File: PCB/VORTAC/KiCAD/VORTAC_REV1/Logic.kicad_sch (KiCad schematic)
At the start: 36 parts, among them Q3 WSD4066DN, U1 TLV73333PDBV, U4 TPS54335ADRCR

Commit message: hallo
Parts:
- removed C? (x3): 0.1uF 16V, Capacitor_SMD:C_0402_1005Metric, symbol Device:C_Small
- removed Q3: WSD4066DN, ToolChanger:WSD4066DN_ThermalPad, symbol ToolChanger:WSD4066DN
- removed R12, R13, R41, R42, R43, R44, R47, R48, R49, R50: 10K, Resistor_SMD:R_0402_1005Metric, symbol Device:R_Small
- removed R7, R8: 100R, Resistor_SMD:R_0402_1005Metric, symbol Device:R_Small
- added R1, R7: 1K, Resistor_SMD:R_0603_1608Metric, symbol Device:R
- added R2, R8: 2K, Resistor_SMD:R_0603_1608Metric, symbol Device:R
- added R5, R6: 180, Resistor_SMD:R_0603_1608Metric, symbol Device:R
- added S1, S2: ~, ToolChanger:OPB666N, symbol VORTAC_REV1-rescue:OPB666N
- R51: value 10K -> 1K
- gave numbers to parts that had none: 11
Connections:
- net +3V3: now also R5.1, R6.1
- net +5V: now also S1.3 (Vc), S2.3 (Vc)
- net GND: now also R2.2, R8.2, S1.1 (AN), S1.5 (GND), S2.1 (AN), S2.5 (GND)
- net TOOL_ID: now also R51.1; no longer C49.2, R51.2
- net TOOL_ID_PIN: now also C49.2, R51.2; no longer R51.1
- new net: R5.2, S2.2 (CA)
- new net: R7.1, S2.4 (Out)
- new net: R1.1, S1.4 (Out)
- new net: R6.2, S1.2 (CA)
- new net ENDSTOP_X: R7.2, R8.1
- new net ENDSTOP_Z: R1.2, R2.1
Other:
- note removed: "LED/USB MOSFET - WSD4066DN"
- moved on the sheet: C49, R51, R52

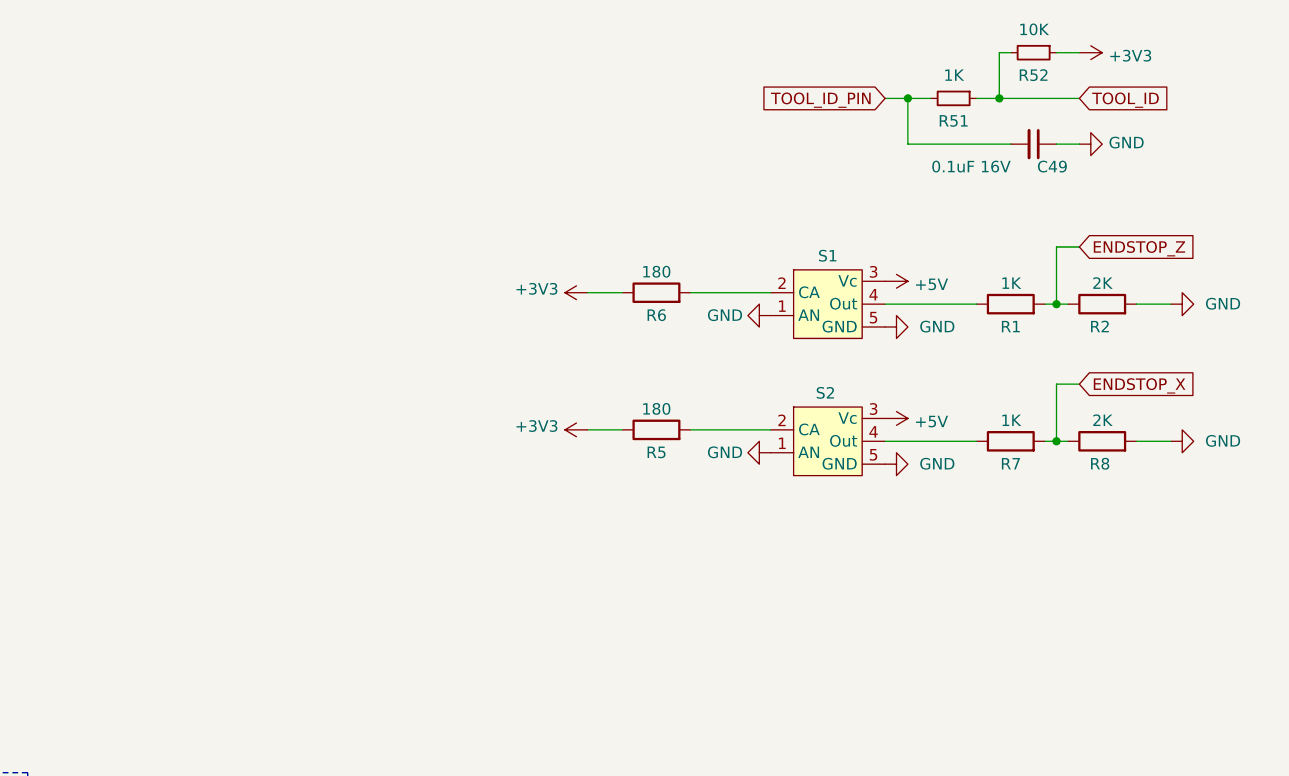
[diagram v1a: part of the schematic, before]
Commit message: Added New EE_SX3350
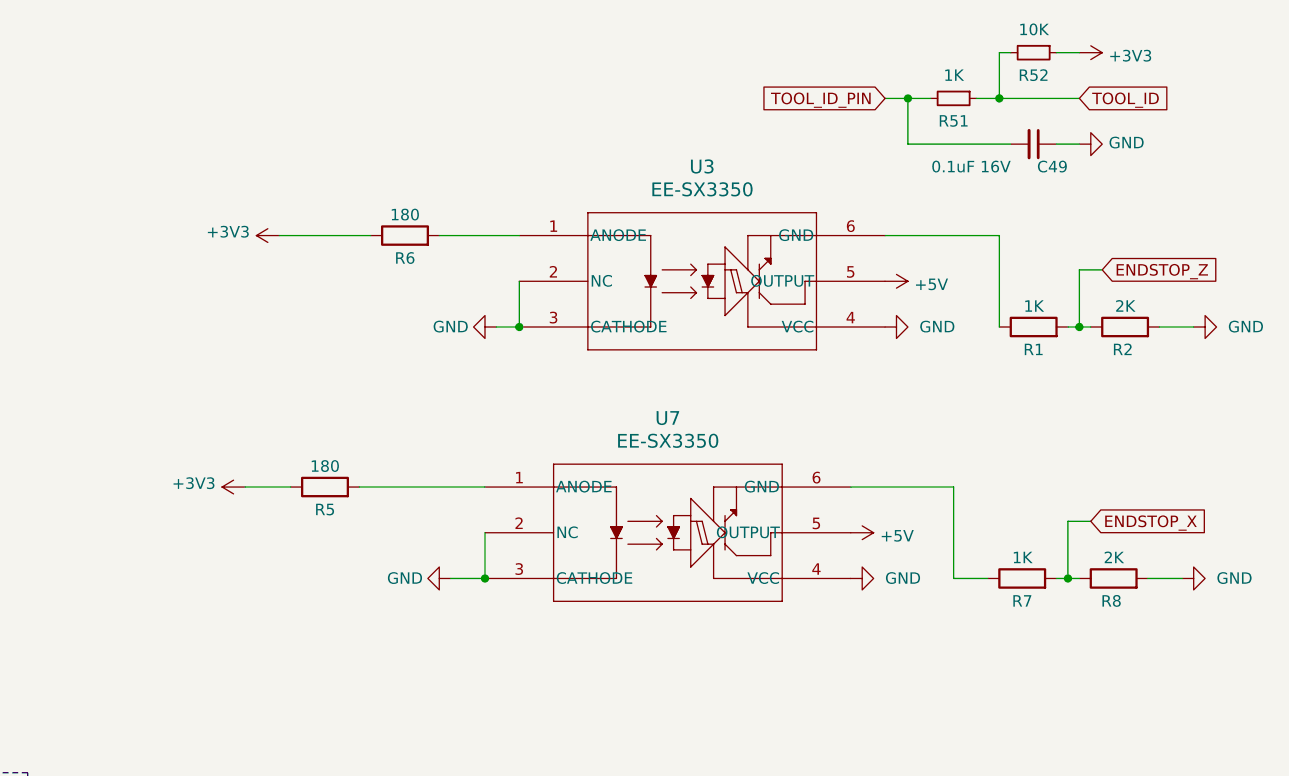
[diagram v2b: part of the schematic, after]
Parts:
- removed S1, S2: ~, ToolChanger:OPB666N, symbol VORTAC_REV1-rescue:OPB666N
- added U3, U7: EE-SX3350, ToolChanger:SENSOR_EE-SX3350_OMR, symbol VORTAC_REV1-rescue:EE-SX3350
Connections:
- net +5V: now also U3.5 (OUTPUT), U7.5 (OUTPUT)
- net GND: now also U3.2 (NC), U3.3 (CATHODE), U3.4 (VCC), U7.2 (NC), U7.3 (CATHODE), U7.4 (VCC)
- net at R5.2: now also U7.1 (ANODE)
- net at R7.1: now also U7.6 (GND)
- net at R1.1: now also U3.6 (GND)
- net at R6.2: now also U3.1 (ANODE)
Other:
- moved on the sheet: R1, R2, R5, R6, R7, R8

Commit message: yipppieee
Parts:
- U3, U7: LCSC (none) -> C7470740
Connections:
- net +5V: now also U3.4 (VCC), U7.4 (VCC); no longer U3.5 (OUTPUT), U7.5 (OUTPUT)
- net GND: now also U3.6 (GND), U7.6 (GND); no longer U3.4 (VCC), U7.4 (VCC)
- net at R7.1: now also U7.5 (OUTPUT); no longer U7.6 (GND)
- net at R1.1: now also U3.5 (OUTPUT); no longer U3.6 (GND)
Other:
- moved on the sheet: C49, R1, R2, R5, R51, R52, R6, R7, R8, U3, U7

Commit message: Fixed Library stuff
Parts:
- L2: footprint ToolChanger:L_Sunlord_MWSA0518_5.4x5.2mm -> Vortac:L_Sunlord_MWSA0518_5.4x5.2mm; LCSC C408412 -> C436530; LCSC ALT C436530 -> (none)
- U3, U7: footprint ToolChanger:SENSOR_EE-SX3350_OMR -> Vortac:SENSOR_EE-SX3350_OMR
- U4: footprint ToolChanger:VSON-10-1EP_3x3mm_P0.5mm_EP1.65x2.4mm_ThermalVias -> Vortac:VSON-10-1EP_3x3mm_P0.5mm_EP1.65x2.4mm_ThermalVias
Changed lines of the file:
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@@
 			)
 		)
-		(property "Footprint" "ToolChanger:L_Sunlord_MWSA0518_5.4x5.2mm"
+		(property "Footprint" "Vortac:L_Sunlord_MWSA0518_5.4x5.2mm"
 			(at 82.55 116.84 0)
 			(effects
@@
 			)
 		)
-		(property "LCSC" "C408412"
-			(at 82.55 116.84 90)
-			(effects
-				(font
-					(size 1.27 1.27)
-				)
-				(hide yes)
-			)
-		)
-		(property "LCSC ALT" "C436530"
+		(property "LCSC" "C436530"
 			(at 82.55 116.84 90)
 			(effects
@@
 			)
 		)
-		(property "Footprint" "ToolChanger:VSON-10-1EP_3x3mm_P0.5mm_EP1.65x2.4mm_ThermalVias"
+		(property "Footprint" "Vortac:VSON-10-1EP_3x3mm_P0.5mm_EP1.65x2.4mm_ThermalVias"
 			(at 66.04 133.35 0)
 			(effects
@@
 			)
 		)
-		(property "Footprint" "ToolChanger:SENSOR_EE-SX3350_OMR"
+		(property "Footprint" "Vortac:SENSOR_EE-SX3350_OMR"
 			(at 214.884 67.564 0)
 			(effects
@@
 			)
 		)
-		(property "Footprint" "ToolChanger:SENSOR_EE-SX3350_OMR"
+		(property "Footprint" "Vortac:SENSOR_EE-SX3350_OMR"
 			(at 214.884 44.704 0)
 			(effects

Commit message: pls merge Jenno
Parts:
- added C15: 0.1uF 50V, Capacitor_SMD:C_0603_1608Metric, symbol Device:C_Small
- added U5: AS5047D, Package_SO:TSSOP-14_4.4x5mm_P0.65mm, symbol Sensor_Magnetic:AS5047D
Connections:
- net +3V3: now also C15.2, U5.11 (VDD), U5.12 (VDD3V3)
- net GND: now also C15.1, U5.13 (GND), U5.5 (TST)
- new net AS_CLK: U5.2 (CLK)
- new net AS_CS: U5.1 (~{CS})
- new net AS_MISO: U5.3 (MISO)
- new net AS_MOSI: U5.4 (MOSI)
- no-connect marks 1 -> 7
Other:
- note added: "Magnetic Angle Sensor (IC using two internal hall sensors)"
- note added: "Optical Endstops (endstop doubles as bed prope)"
- note added: "TOOL ID (sense pin)"
- moved on the sheet: C11, C12, C14, C16, C18, C20, C3, C49, C5, C7, C8, L2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

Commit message: Liebe Griasse zurrueck
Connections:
- net AS_CS renamed AS_NCS
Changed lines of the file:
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@@
 		)
 	)
-	(global_label "AS_CS"
+	(global_label "AS_NCS"
 		(shape input)
 		(at 40.64 167.64 180)
@@
 			)
 		)
-		(property "Datasheet" "https://ams.com/documents/20143/36005/AS5047D_DS000394_2-00.pdf"
+		(property "Datasheet" "https://www.lcsc.com/datasheet/lcsc_datasheet_2504101957_AMS-AS5047D-ATSM_C2693743.pdf"
 			(at 41.91 181.61 0)
 			(effects

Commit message: Gschenkle
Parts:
- removed R2, R8: 2K, Resistor_SMD:R_0603_1608Metric, symbol Device:R
- added C19, C25: 0.1uF 16V, Capacitor_SMD:C_0402_1005Metric, symbol Device:C_Small
- added R14, R2, R8: 10K, Resistor_SMD:R_0402_1005Metric, symbol Device:R_Small
- R5, R6: value 180 -> 330R
- U3, U7: value EE-SX3350 -> EE-SX4350; LCSC C7470740 -> C17524058
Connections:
- net +3V3: now also R14.2, R2.1, R8.1; no longer R5.1, R6.1
- net +5V: now also R5.1, R6.1
- net ENDSTOP_X: now also C25.2, R8.2
- net ENDSTOP_Z: now also C19.2, R2.2
- net GND: now also C19.1, C25.1
- net AS_CLK renamed AS_SCK
- net AS_NCS renamed AS_NSS
- net AS_NSS: now also R14.1
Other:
- moved on the sheet: R1, R5, R6, R7, U3, U7

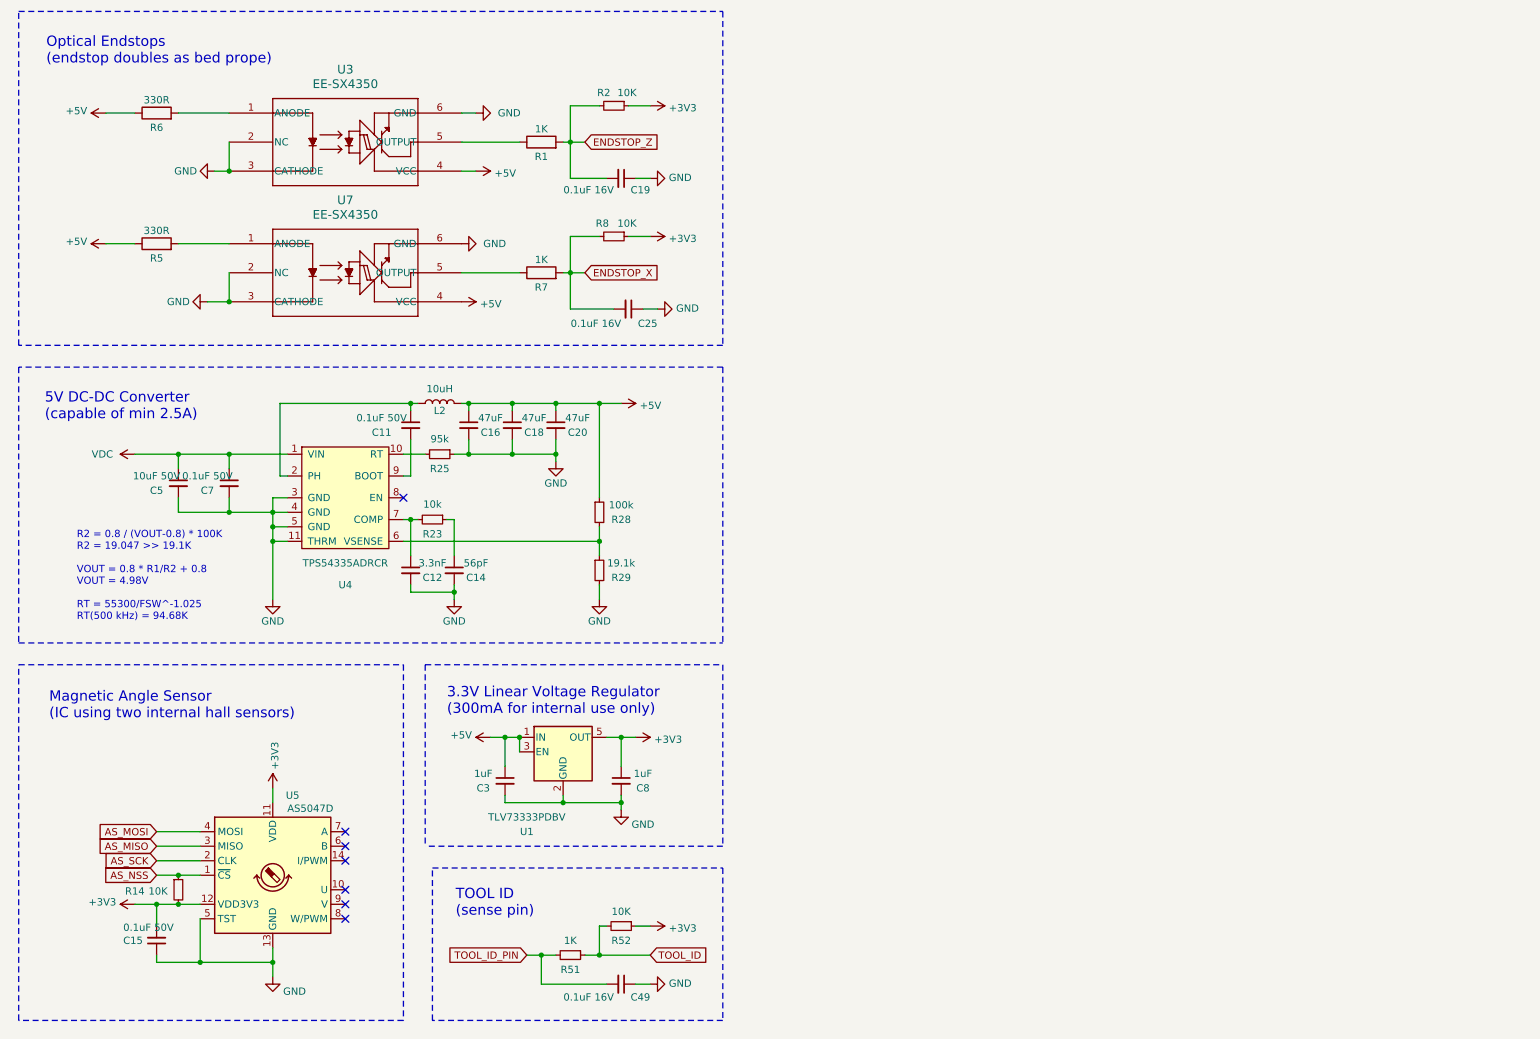
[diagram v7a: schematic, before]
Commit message: Schematic updates
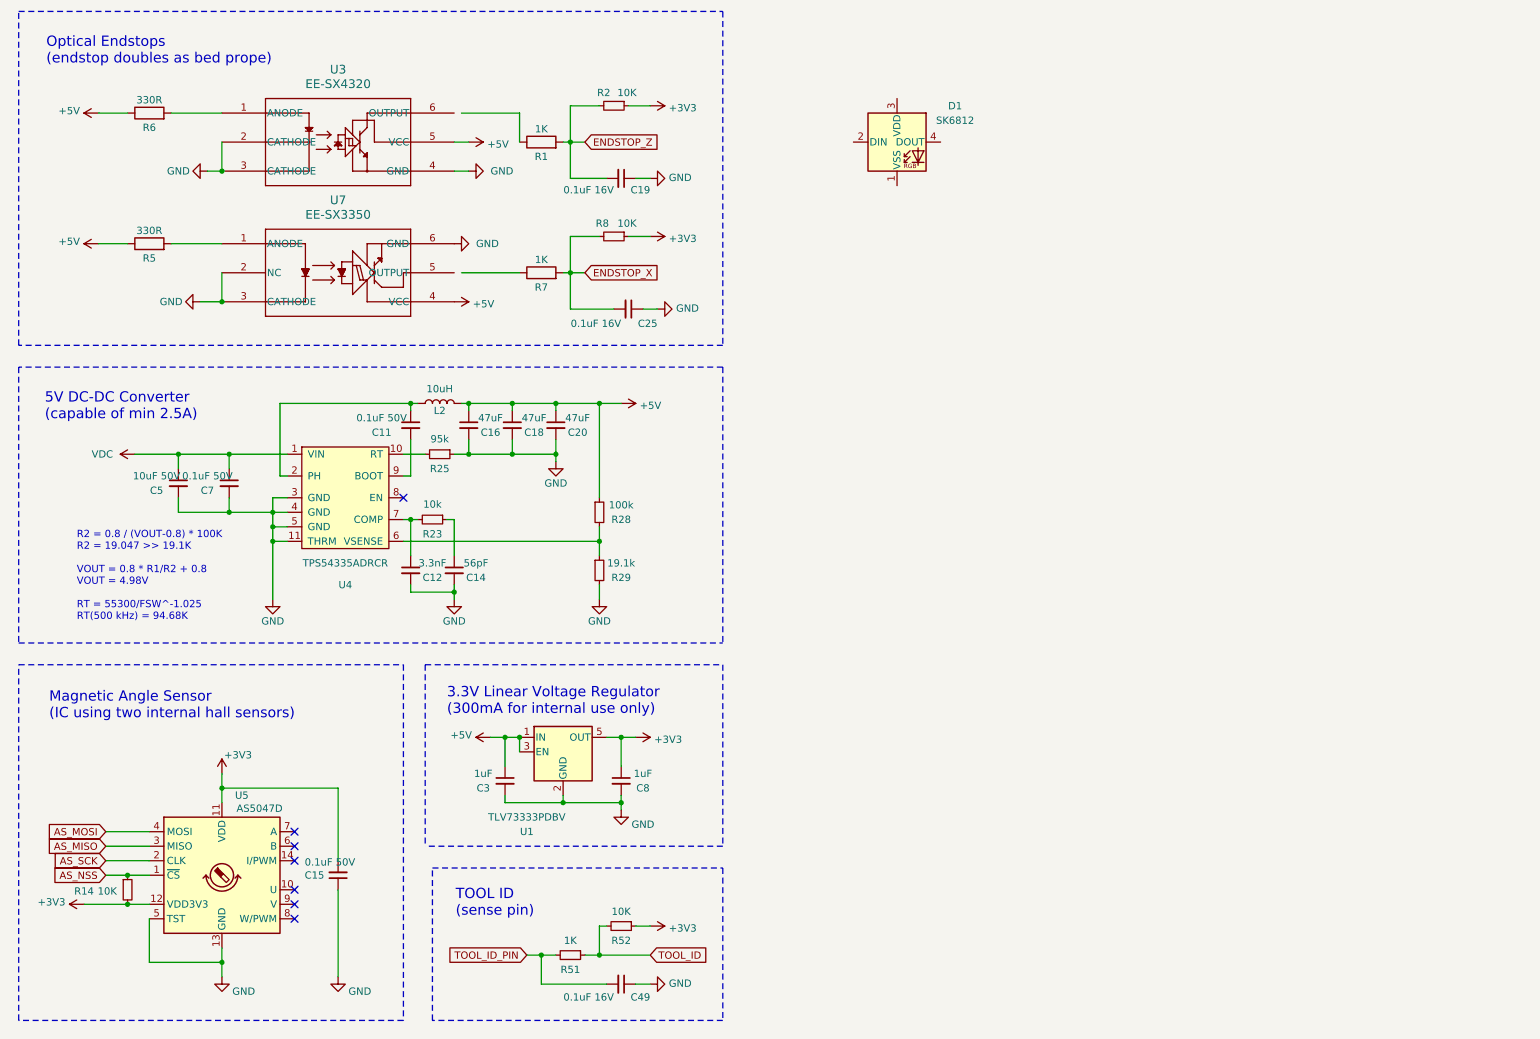
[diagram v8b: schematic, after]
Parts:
- removed U3: EE-SX4350, Vortac:SENSOR_EE-SX3350_OMR, symbol VORTAC_REV1-rescue:EE-SX3350
- added D1: SK6812, LED_SMD:LED_SK6812_PLCC4_5.0x5.0mm_P3.2mm, symbol LED:SK6812
- added U3: EE-SX4320, Vortac:SENSOR_EE-SX4320_OMR, symbol Vortac:EE-SX4320
- U7: value EE-SX4350 -> EE-SX3350; LCSC C17524058 -> C7470740
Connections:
- net +5V: now also U3.5 (VCC)
- net GND: now also U3.2 (CATHODE), U3.3 (CATHODE), U3.4 (GND)
- net at R7.1: no longer U7.5 (OUTPUT)
- net at R6.2: now also U3.1 (ANODE)
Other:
- moved on the sheet: C15, R14, R5, R6, U5, U7
